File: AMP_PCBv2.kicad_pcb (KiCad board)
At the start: 2 copper layers, 100.1 x 100.1 mm, 116 parts, among them J1 POWER, J2 EBRAKE, J3 MC, J4 STEERING, J5 OLED Breakout, J6 EBRAKE_BREAKOUT, Q1 Q_NMOS_GDS, Q2 Q_NMOS_GDS, Q3 Q_NMOS_GDS, Q4 Q_NMOS_GDS, U1 Teensy4.0, U10 RFM9x, U2 FT234XD, U3 LM1117-ADJ, U4 LM1117-ADJ, U5 74HC157, U6 74HC157, U7 74HC4060, U8 74HC00, U9 TLV272

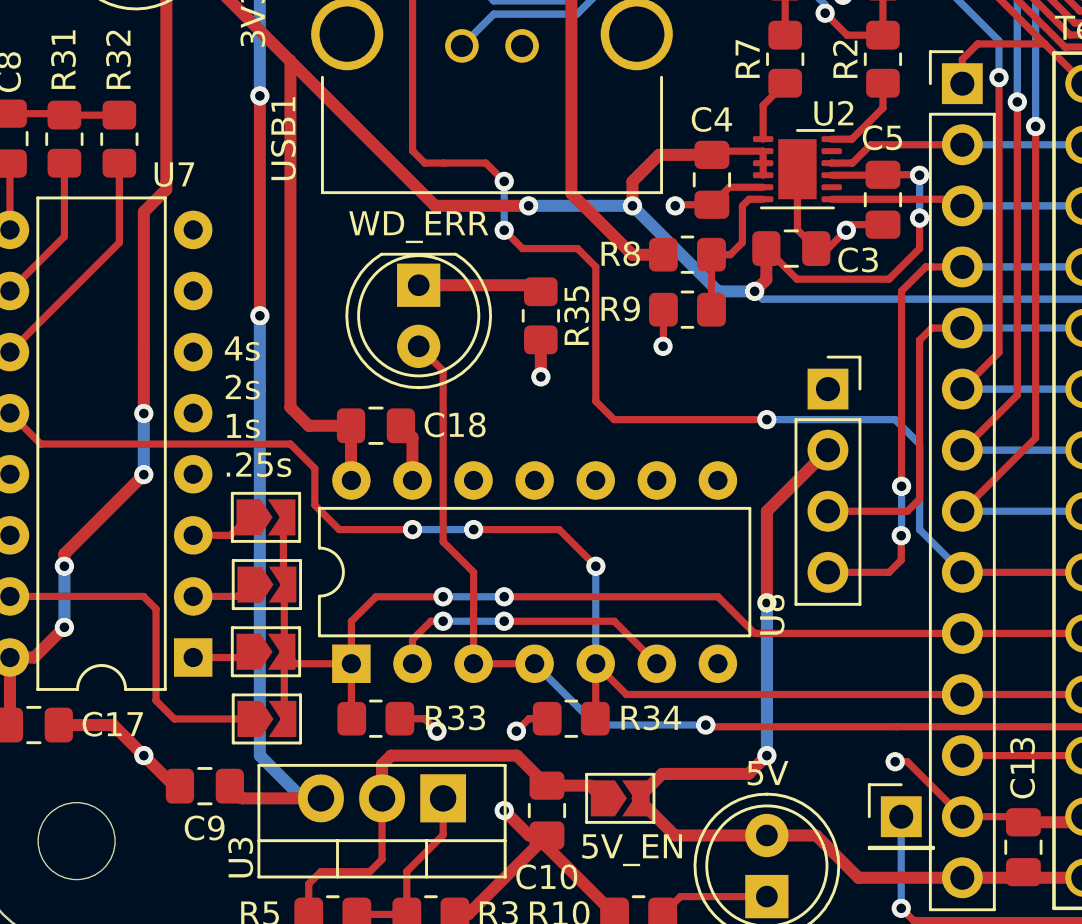
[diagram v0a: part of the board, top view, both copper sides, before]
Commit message: Add OLED connector labels #9
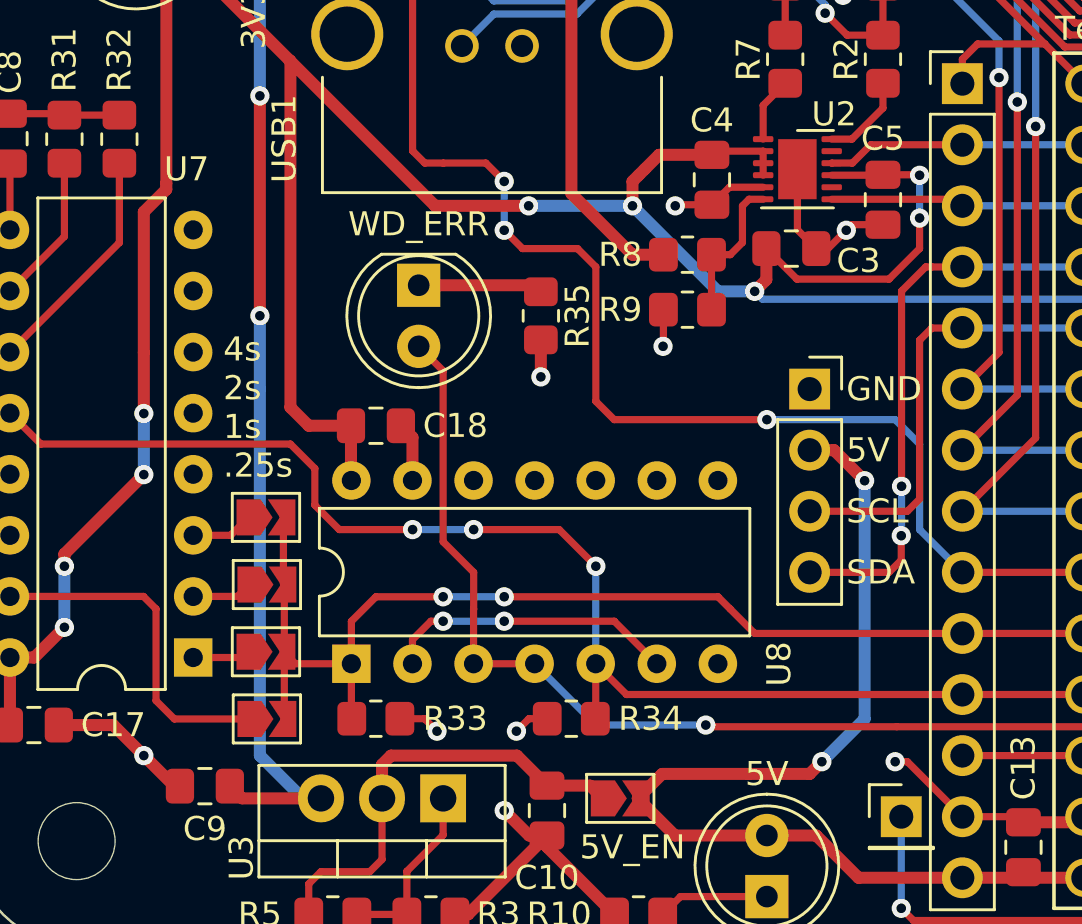
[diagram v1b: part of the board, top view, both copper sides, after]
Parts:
- moved J5 0.76 mm to (122.2, 124.5)
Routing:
- net +5V: track 40.0 -> 43.7 mm
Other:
- board text added: "SCL"
- board text added: "SDA"
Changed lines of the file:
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@@
     (property "Sheetname" "")
     (attr through_hole)
-    (fp_text reference "U8" (at 2.022 17.531 270) (layer "F.SilkS")
+    (fp_text reference "U8" (at -0.01 17.785 270) (layer "F.SilkS")
       (effects (font (size 1 1) (thickness 0.15)))
     )
@@
   )
   (footprint "Connector_PinSocket_2.54mm:PinSocket_1x04_P2.54mm_Vertical" (layer "F.Cu")
-    (at 122.936 124.46)
+    (at 122.174 124.46)
     (descr "Through hole straight socket strip, 1x04, 2.54mm pitch, single row (from Kicad 4.0.7), script generated")
     (tags "Through hole socket strip THT 1x04 2.54mm single row")
@@
     (property "Sheetname" "")
     (attr through_hole)
-    (fp_text reference "U7" (at 0.7835 20.051) (layer "F.SilkS")
+    (fp_text reference "U7" (at 0.2755 20.305) (layer "F.SilkS")
       (effects (font (size 1 1) (thickness 0.15)))
     )
@@
     (effects (font (size 1 1) (thickness 0.15)))
   )
+  (gr_text "5V" (at 123.698 127) (layer "F.SilkS")
+    (effects (font (size 1 1) (thickness 0.15)) (justify left))
+  )
   (gr_text "GND" (at 184.912 139.446) (layer "F.SilkS")
     (effects (font (size 1 1) (thickness 0.15)))
@@
     (effects (font (size 1 1) (thickness 0.15)))
   )
+  (gr_text "SDA" (at 123.698 132.08) (layer "F.SilkS")
+    (effects (font (size 1 1) (thickness 0.15)) (justify left))
+  )
   (gr_text "REV" (at 172.725 95.504) (layer "F.SilkS")
     (effects (font (size 1 1) (thickness 0.15)))
@@
     (effects (font (size 1 1) (thickness 0.15)))
   )
+  (gr_text "GND" (at 123.698 124.46) (layer "F.SilkS")
+    (effects (font (size 1 1) (thickness 0.15)) (justify left))
+  )
   (gr_text "5V_EN" (at 114.808 143.51) (layer "F.SilkS")
     (effects (font (size 1 1) (thickness 0.15)))
@@
     (effects (font (size 1 1) (thickness 0.15)))
   )
+  (gr_text "SCL" (at 123.698 129.54) (layer "F.SilkS")
+    (effects (font (size 1 1) (thickness 0.15)) (justify left))
+  )
   (gr_text "| FS1\n| FWD\n| REV\n| THROTTLE\n| FB\n| EBRAKE1\n| EBRAKE2\n| STEERING" (at 88.9 64.008) (layer "F.SilkS")
     (effects (font (size 1 1) (thickness 0.15)) (justify left))
@@
   (segment (start 99.314 124.46) (end 99.314 121.412) (width 0.5) (layer "B.Cu") (net 9))
   (segment (start 122.448 143.022) (end 124.206 144.78) (width 0.5) (layer "F.Cu") (net 10))
-  (segment (start 120.396 133.35) (end 120.396 129.54) (width 0.5) (layer "F.Cu") (net 10))
+  (segment (start 122.174 127) (end 123.19 127) (width 0.5) (layer "F.Cu") (net 10))
+  (segment (start 122.174 140.462) (end 122.682 139.954) (width 0.5) (layer "F.Cu") (net 10))
   (segment (start 130.8315 144.78) (end 131.064 144.5475) (width 0.5) (layer "F.Cu") (net 10))
+  (segment (start 119.634 140.462) (end 122.174 140.462) (width 0.5) (layer "F.Cu") (net 10))
   (segment (start 120.396 143.022) (end 116.569 143.022) (width 0.5) (layer "F.Cu") (net 10))
   (segment (start 131.2965 144.78) (end 131.064 144.5475) (width 0.5) (layer "F.Cu") (net 10))
@@
   (segment (start 133.604 144.78) (end 131.2965 144.78) (width 0.5) (layer "F.Cu") (net 10))
   (segment (start 124.206 144.78) (end 128.524 144.78) (width 0.5) (layer "F.Cu") (net 10))
-  (segment (start 122.936 127) (end 120.396 129.54) (width 0.5) (layer "F.Cu") (net 10))
   (segment (start 116.041 140.462) (end 115.025 141.478) (width 0.5) (layer "F.Cu") (net 10))
+  (segment (start 123.19 127) (end 124.46 128.27) (width 0.5) (layer "F.Cu") (net 10))
   (segment (start 116.569 143.022) (end 115.025 141.478) (width 0.5) (layer "F.Cu") (net 10))
-  (segment (start 120.396 139.7) (end 119.634 140.462) (width 0.5) (layer "F.Cu") (net 10))
-  (via (at 120.396 133.35) (size 0.8) (drill 0.4) (layers "F.Cu" "B.Cu") (net 10))
-  (via (at 120.396 139.7) (size 0.8) (drill 0.4) (layers "F.Cu" "B.Cu") (net 10))
-  (segment (start 120.396 133.35) (end 120.396 139.7) (width 0.5) (layer "B.Cu") (net 10))
+  (via (at 124.46 128.27) (size 0.8) (drill 0.4) (layers "F.Cu" "B.Cu") (net 10))
+  (via (at 122.682 139.954) (size 0.8) (drill 0.4) (layers "F.Cu" "B.Cu") (net 10))
+  (segment (start 122.682 139.954) (end 124.46 138.176) (width 0.5) (layer "B.Cu") (net 10))
+  (segment (start 124.46 138.176) (end 124.46 128.27) (width 0.5) (layer "B.Cu") (net 10))
   (segment (start 92.17 89.122) (end 91.186 88.138) (width 0.5) (layer "F.Cu") (net 11))
   (segment (start 95.758 89.122) (end 92.17 89.122) (width 0.5) (layer "F.Cu") (net 11))

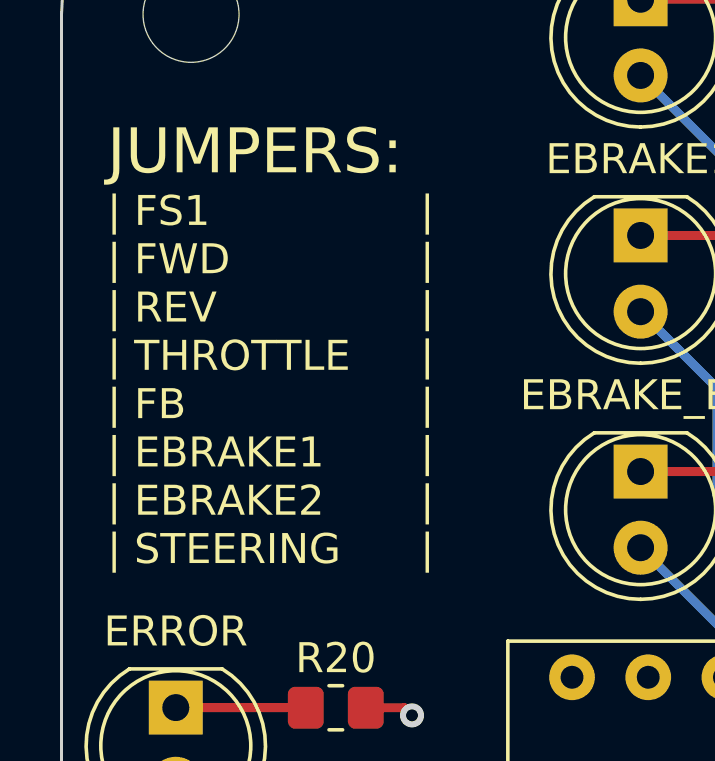
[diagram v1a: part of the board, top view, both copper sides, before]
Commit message: Fix jumper label text #6
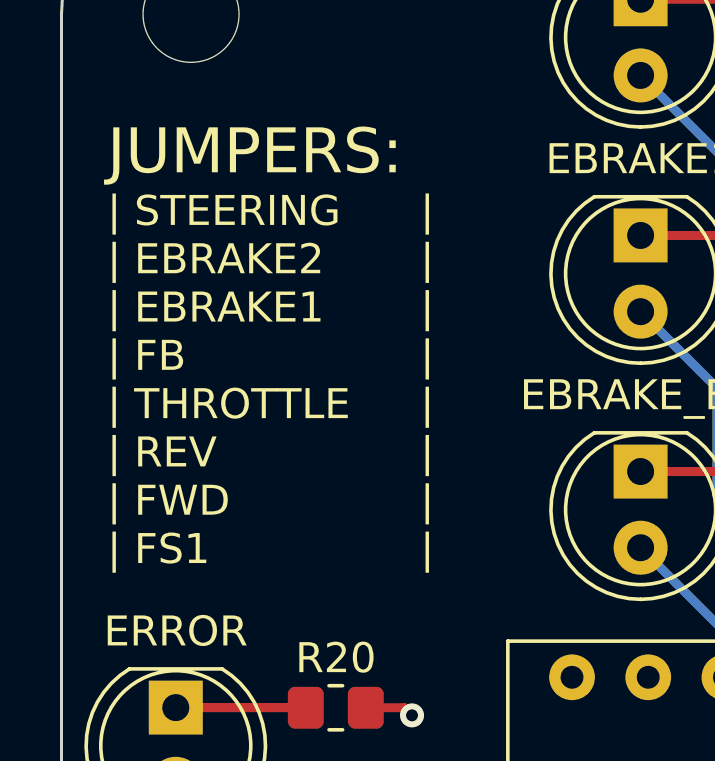
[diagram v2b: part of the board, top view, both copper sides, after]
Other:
- board text added: "| STEERING | EBRAKE2 | EBRAKE1 | FB | THROTTLE | REV | FWD | FS1"
- board text removed: "| FS1 | FWD | REV | THROTTLE | FB | EBRAKE1 | EBRAKE2 | STEERING"
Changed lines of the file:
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@@
     (effects (font (size 1 1) (thickness 0.15)) (justify left))
   )
-  (gr_text "| FS1\n| FWD\n| REV\n| THROTTLE\n| FB\n| EBRAKE1\n| EBRAKE2\n| STEERING" (at 88.9 64.008) (layer "F.SilkS")
+  (gr_text "| STEERING\n| EBRAKE2\n| EBRAKE1\n| FB\n| THROTTLE\n| REV\n| FWD\n| FS1" (at 88.9 64.008) (layer "F.SilkS")
     (effects (font (size 1 1) (thickness 0.15)) (justify left))
   )

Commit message: Change PCB info text to be relative to KiCad file
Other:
- board text added: "${TITLE} Revision ${REVISION} ${ISSUE_DATE}"
- board text removed: "AMP PCBv2 Revision B 2023-01-11"
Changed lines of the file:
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@@
   (title_block
     (title "AMP PCBv2")
-    (date "2023-01-11")
+    (date "2023-01-13")
     (rev "B")
     (company "Autonomous Motorsports Purdue")
@@
   (gr_line (start 187.452 51.816) (end 187.452 143.256) (layer "Edge.Cuts") (width 0.1))
   (gr_arc (start 91.694 147.574) (mid 88.640713 146.309287) (end 87.376 143.256) (layer "Edge.Cuts") (width 0.1))
-  (gr_text "AMP PCBv2\nRevision B\n2023-01-11" (at 147.574 77.978) (layer "B.SilkS")
+  (gr_text "${TITLE}\nRevision ${REVISION}\n${ISSUE_DATE}" (at 147.574 77.978) (layer "B.SilkS")
     (effects (font (size 2 2) (thickness 0.3)) (justify mirror))
   )
